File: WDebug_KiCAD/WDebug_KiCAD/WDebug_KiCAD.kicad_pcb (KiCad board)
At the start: 2 copper layers, 55 x 34 mm, 49 parts, among them J1 USB_C_Receptacle_USB2.0, J2 HD2*10, J3 20p, J4 18p, SW1 sw, U1 USB2514B_Bi, U2 CH340E, U3 CH340E, U4 SPX3819M5-L, Y1 24MHz

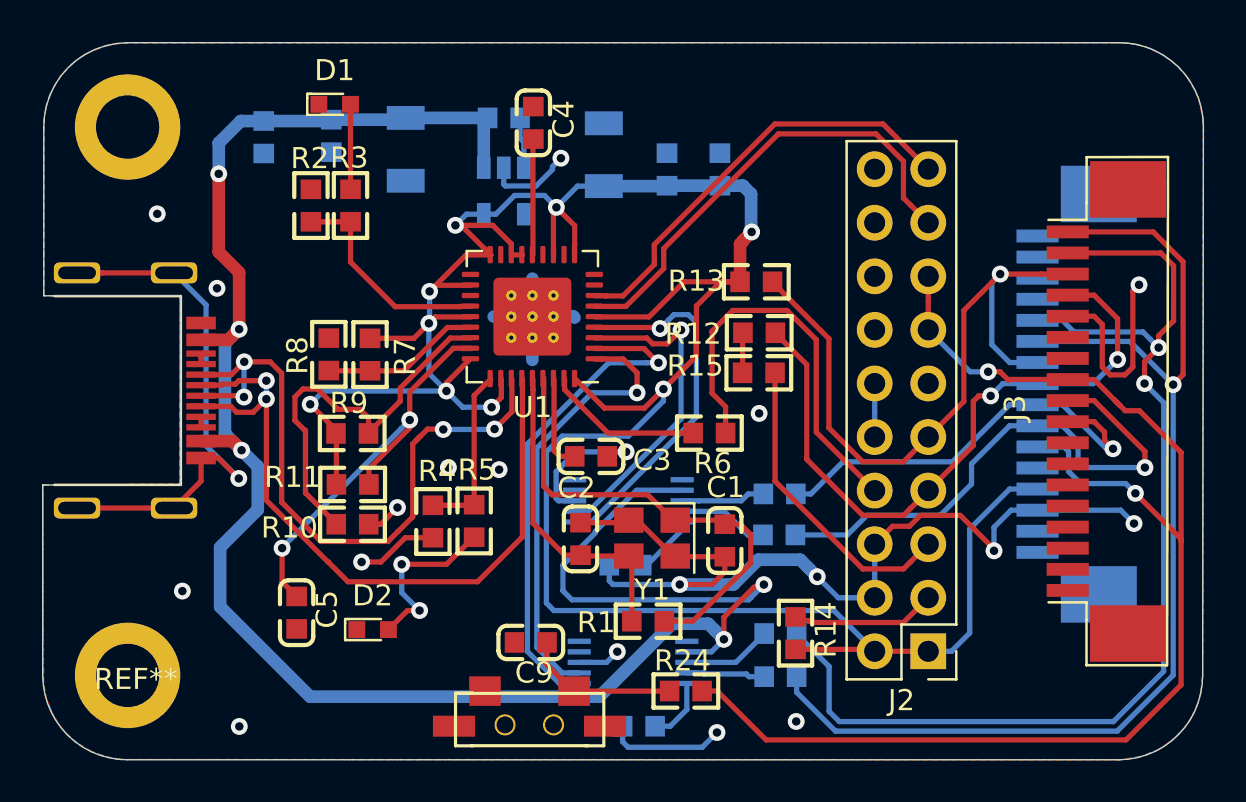
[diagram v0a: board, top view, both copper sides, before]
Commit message: 修正DAPlink 1.5版本 串口信号修改，新加一路串口
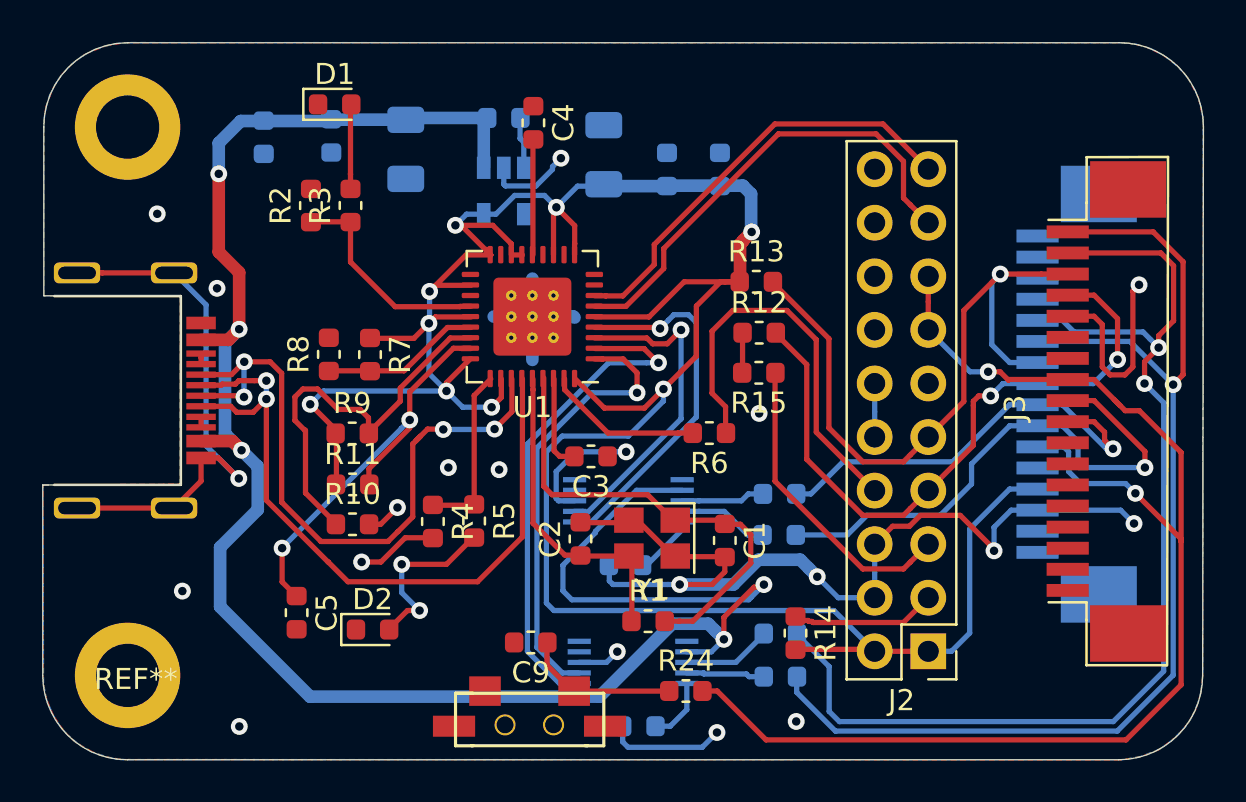
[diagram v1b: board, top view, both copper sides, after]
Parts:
- C1, C10, C11, C13, C14, C2, C3, C4, C5, C6, C7, C9: footprint lc_lib:0603_C -> Capacitor_SMD:C_0603_1608Metric
- C12, C8: footprint lc_lib:1206_C -> Capacitor_SMD:C_1206_3216Metric
- D1, D2: footprint digikey-footprints:LED_0603 -> LED_SMD:LED_0603_1608Metric
- R1, R10, R11, R12, R13, R14, R15, R16, R17, R18, R19, R2, R24, R25, R3, R4, R5, R6, R7, R8, R9: footprint lc_lib:0603_R -> Resistor_SMD:R_0603_1608Metric
